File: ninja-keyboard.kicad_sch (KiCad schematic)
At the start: 143 parts, among them J1 USB_C_Receptacle_USB2.0_14P, J2 Conn_01x02, Q1 AO3401A, SW1 backquote, SW10 num9, SW11 num0, SW12 -, SW13 =, SW14 backsapce, SW15 tab, SW16 q, SW17 w, SW18 e, SW19 r, SW2 num1, SW20 t, SW21 y, SW22 u, SW23 i, SW24 o, SW25 p, SW26 [, SW27 ], SW28 \, SW29 cap, SW3 num2, SW30 a, SW31 s, SW32 d, SW33 f, SW34 h, SW35 g, SW36 j, SW37 k, SW38 l, SW39 semicolon, SW4 num3, SW40 apostrophe, SW41 enter, SW42 pgdown, SW43 lshift, SW44 z, SW45 x, SW46 c, SW47 v, SW48 b, SW49 n, SW5 num4, SW50 m, SW51 comma, SW52 period, SW53 /, SW54 rshift, SW55 up, SW56 end, SW57 lctrl, SW58 win, SW59 lalt, SW6 num5, SW60 lfn, SW61 space, SW62 macro, SW63 rfn, SW64 ralt, SW65 rctrl, SW66 left, SW67 down, SW68 right, SW69 pgup, SW7 num6, SW70 home, SW8 num7, SW9 num8, U1 ESP32-S3-WROOM-1, U2 AMS1117-3.3, U3 TP4056-42-ESOP8

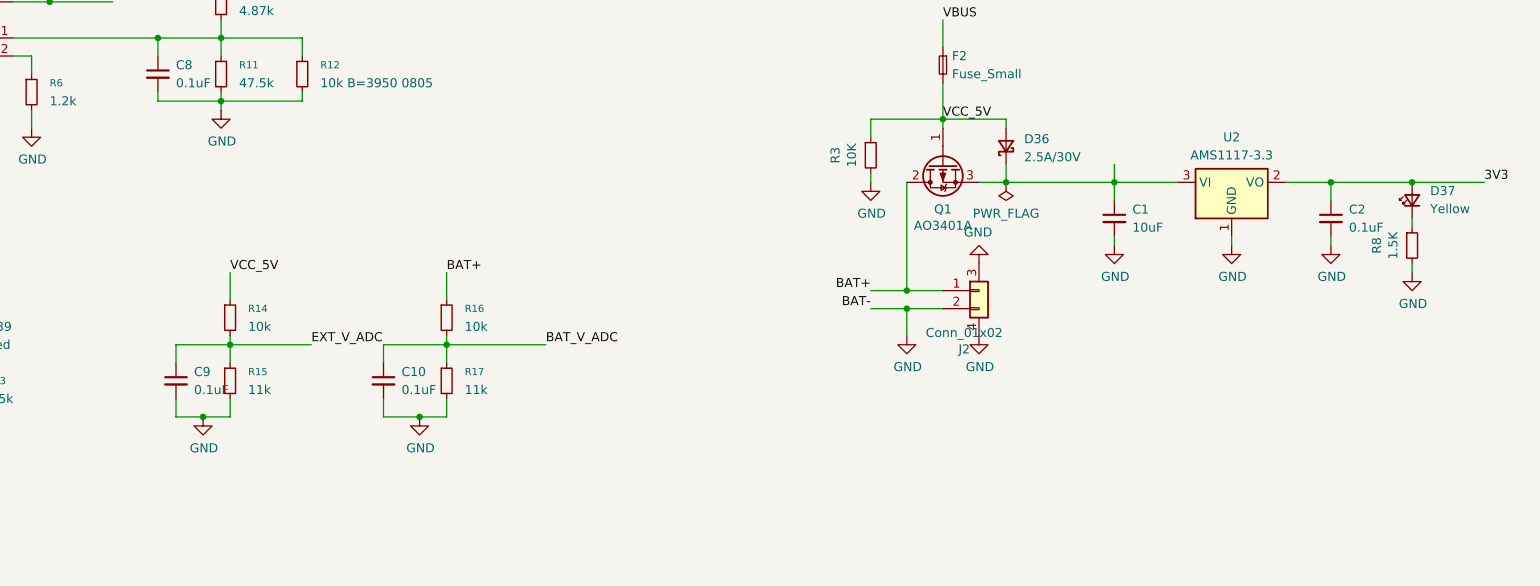
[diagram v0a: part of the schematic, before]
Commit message: Lay the components on the board, but haven't connect them with traces
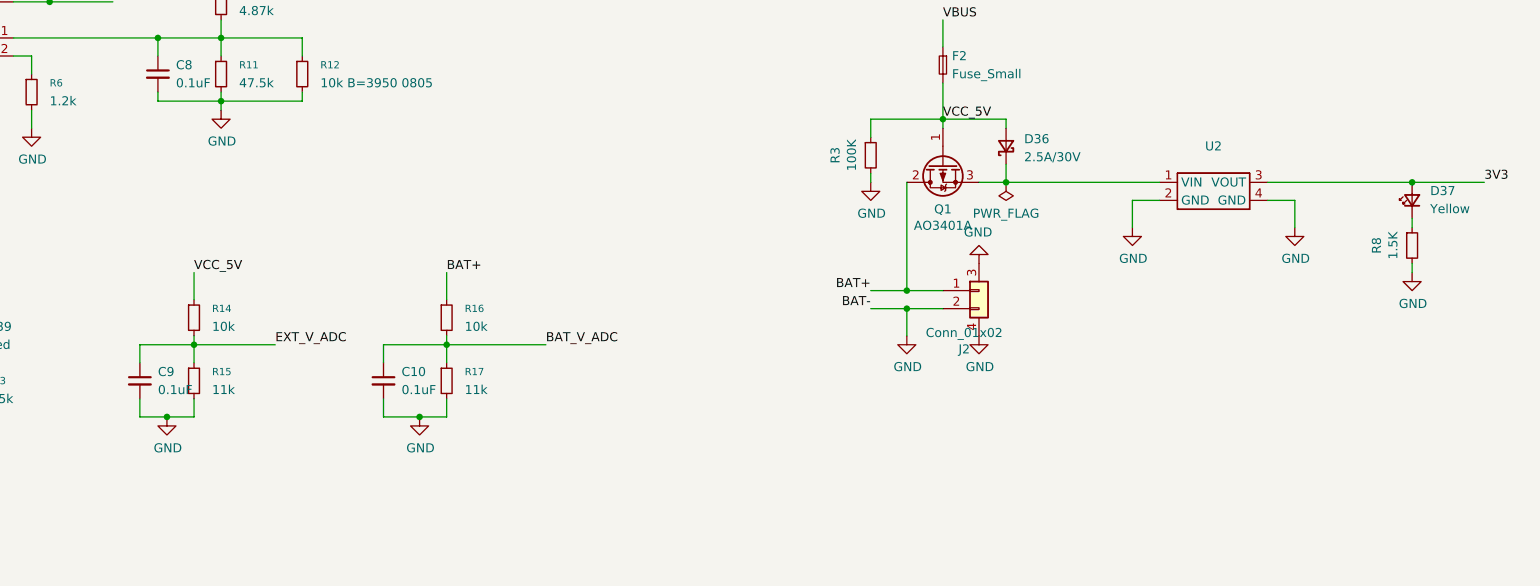
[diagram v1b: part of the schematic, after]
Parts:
- removed C1: 10uF, Capacitor_SMD:C_0603_1608Metric, symbol Device:C_Small
- removed C2: 0.1uF, Capacitor_SMD:C_0603_1608Metric, symbol Device:C_Small
- removed U2: AMS1117-3.3, Package_TO_SOT_SMD:SOT-223-3_TabPin2, symbol Regulator_Linear:AMS1117-3.3
- added U2: ~, user_added:XL63020-3.3, symbol user_created:XL63020-3.3
- R3: value 10K -> 100K
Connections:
- net 3V3: now also U2.3 (VOUT)
- net GND: now also U2.2 (GND), U2.4 (GND)
- net at D36.1 (K), Q1.3 (S): now also U2.1 (VIN)
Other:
- moved on the sheet: C9, R14, R15

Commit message: commit before trying to fix stuck kicad
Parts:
- SW1, SW10, SW11, SW12, SW13, SW16, SW17, SW18, SW19, SW2, SW20, SW21, SW22, SW23, SW24, SW25, SW26, SW27, SW3, SW30, SW31, SW32, SW33, SW34, SW35, SW36, SW37, SW38, SW39, SW4, SW40, SW42, SW44, SW45, SW46, SW47, SW48, SW49, SW5, SW50, SW51, SW52, SW53, SW55, SW56, SW6, SW60, SW63, SW66, SW67, SW68, SW69, SW7, SW70, SW8, SW9: symbol Switch:SW_Push -> user_created:SW_Push with Smart LED
- SW14, SW29: footprint PCM_Switch_Keyboard_Hotswap_Kailh:SW_Hotswap_Kailh_MX_1.75u -> user_added:SW_Hotswap_Kailh_MX_1.75u with led; symbol Switch:SW_Push -> user_created:SW_Push with Smart LED
- SW15, SW54: footprint PCM_Switch_Keyboard_Hotswap_Kailh:SW_Hotswap_Kailh_MX_1.50u -> user_added:SW_Hotswap_Kailh_MX_1.50u with led; symbol Switch:SW_Push -> user_created:SW_Push with Smart LED
- SW28, SW57, SW58, SW59, SW64, SW65: footprint PCM_Switch_Keyboard_Hotswap_Kailh:SW_Hotswap_Kailh_MX_1.25u -> user_added:SW_Hotswap_Kailh_MX_1.25u with led; symbol Switch:SW_Push -> user_created:SW_Push with Smart LED
- SW41: footprint PCM_Switch_Keyboard_Hotswap_Kailh:SW_Hotswap_Kailh_MX_2.00u -> user_added:SW_Hotswap_Kailh_MX_2.00u with led; symbol Switch:SW_Push -> user_created:SW_Push with Smart LED
- SW43, SW61, SW62: footprint PCM_Switch_Keyboard_Hotswap_Kailh:SW_Hotswap_Kailh_MX_2.25u -> user_added:SW_Hotswap_Kailh_MX_2.25u with led; symbol Switch:SW_Push -> user_created:SW_Push with Smart LED
- U1: footprint PCM_Espressif:ESP32-S3-WROOM-1U -> PCM_Espressif:ESP32-S3-WROOM-1
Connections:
- net GND: no longer J2.3, J2.4
- net at SW21.1, SW35.1, SW49.1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: now also SW21. (6), SW35. (6), SW49. (6), SW7. (6)
- net at SW20.2, SW34.2, SW48.2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: now also SW20. (6), SW34. (6), SW48. (6), SW6. (6)
- net at SW1.1, SW15.1, SW29.1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: now also SW1. (6), SW15. (6), SW29. (6), SW43. (6)
- net at SW13.1, SW27.1, SW41.1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: now also SW13. (6), SW27. (6), SW41. (6), SW55. (6)
- net at SW19.1, SW33.1, SW47.1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: now also SW19. (6), SW33. (6), SW47. (6), SW5. (6)
- net at SW23.1, SW37.1, SW51.1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: now also SW23. (6), SW37. (6), SW51. (6), SW9. (6)
- net at SW17.1, SW3.1, SW31.1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: now also SW17. (6), SW3. (6), SW31. (6), SW45. (6)
- net at SW14.2, SW28.2, SW42.2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: now also SW14. (6), SW28. (6), SW42. (6), SW56. (6)
- net at SW18.2, SW32.2, SW4.2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: now also SW18. (6), SW32. (6), SW4. (6), SW46. (6)
- net at SW22.2, SW36.2, SW50.2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: now also SW22. (6), SW36. (6), SW50. (6), SW8. (6)
- net at SW11.1, SW25.1, SW39.1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: now also SW11. (6), SW25. (6), SW39. (6), SW53. (6)
- net at SW12.2, SW26.2, SW40.2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: now also SW12. (6), SW26. (6), SW40. (6), SW54. (6)
- net at SW16.2, SW2.2, SW30.2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: now also SW16. (6), SW2. (6), SW30. (6), SW44. (6)
- net at SW10.2, SW24.2, SW38.2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: now also SW10. (6), SW24. (6), SW38. (6), SW52. (6)
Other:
- moved on the sheet: C10, C3, C4, C5, C6, C7, C8, C9, D1, D10, D11, D12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

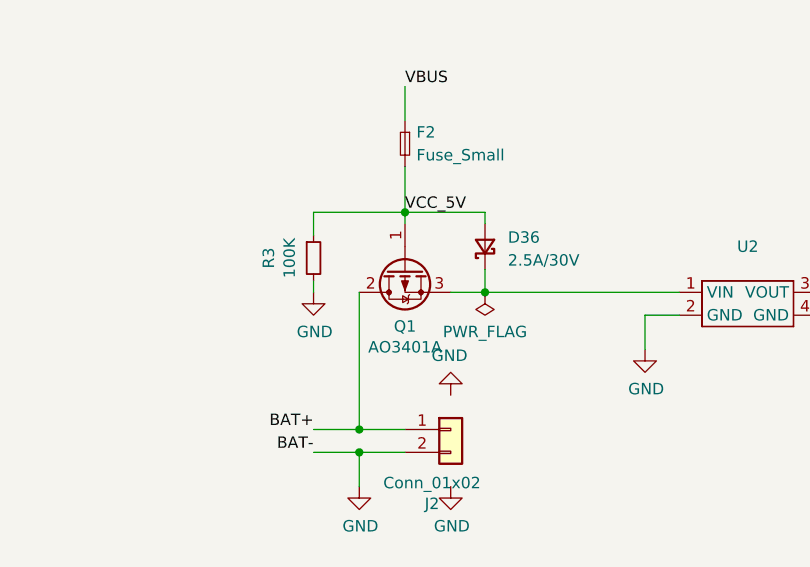
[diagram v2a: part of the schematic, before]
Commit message: use export netlist feature for now
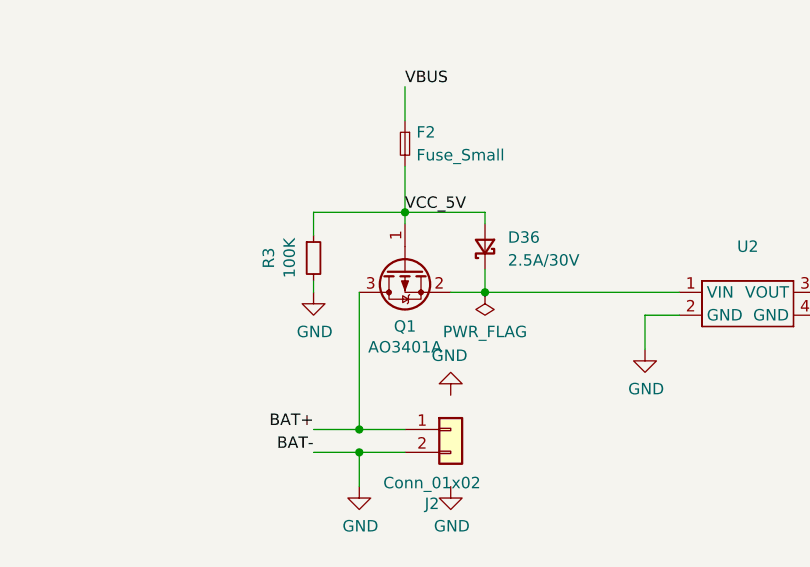
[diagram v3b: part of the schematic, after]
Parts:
- Q1: symbol Device:Q_PMOS_GDS -> Transistor_FET:AO3401A
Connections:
- net BAT+: now also Q1.3 (D); no longer Q1.2 (D)
- net at SW21.1, SW35.1, SW49.1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: now also SW21.3 (VDD), SW21.4 (DOUT), SW35.3 (VDD), SW35.4 (DOUT), SW49.3 (VDD), SW49.4 (DOUT), SW7.3 (VDD), SW7.4 (DOUT); no longer SW21. (6), SW35. (6), SW49. (6), SW7. (6)
- net at SW20.2, SW34.2, SW48.2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: now also SW20.5 (DIN), SW20.6 (GND), SW34.5 (DIN), SW34.6 (GND), SW48.5 (DIN), SW48.6 (GND), SW6.5 (DIN), SW6.6 (GND); no longer SW20. (6), SW34. (6), SW48. (6), SW6. (6)
- net at SW1.1, SW15.1, SW29.1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: now also SW1.3 (VDD), SW1.4 (DOUT), SW15.3 (VDD), SW15.4 (DOUT), SW29.3 (VDD), SW29.4 (DOUT), SW43.3 (VDD), SW43.4 (DOUT); no longer SW1. (6), SW15. (6), SW29. (6), SW43. (6)
- net at D36.1 (K), U2.1 (VIN): now also Q1.2 (S); no longer Q1.3 (S)
- net at SW13.1, SW27.1, SW41.1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: now also SW13.3 (VDD), SW13.4 (DOUT), SW27.3 (VDD), SW27.4 (DOUT), SW41.3 (VDD), SW41.4 (DOUT), SW55.3 (VDD), SW55.4 (DOUT); no longer SW13. (6), SW27. (6), SW41. (6), SW55. (6)
- net at SW19.1, SW33.1, SW47.1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: now also SW19.3 (VDD), SW19.4 (DOUT), SW33.3 (VDD), SW33.4 (DOUT), SW47.3 (VDD), SW47.4 (DOUT), SW5.3 (VDD), SW5.4 (DOUT); no longer SW19. (6), SW33. (6), SW47. (6), SW5. (6)
- net at SW23.1, SW37.1, SW51.1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: now also SW23.3 (VDD), SW23.4 (DOUT), SW37.3 (VDD), SW37.4 (DOUT), SW51.3 (VDD), SW51.4 (DOUT), SW9.3 (VDD), SW9.4 (DOUT); no longer SW23. (6), SW37. (6), SW51. (6), SW9. (6)
- net at SW17.1, SW3.1, SW31.1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: now also SW17.3 (VDD), SW17.4 (DOUT), SW3.3 (VDD), SW3.4 (DOUT), SW31.3 (VDD), SW31.4 (DOUT), SW45.3 (VDD), SW45.4 (DOUT); no longer SW17. (6), SW3. (6), SW31. (6), SW45. (6)
- net at SW14.2, SW28.2, SW42.2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: now also SW14.5 (DIN), SW14.6 (GND), SW28.5 (DIN), SW28.6 (GND), SW42.5 (DIN), SW42.6 (GND), SW56.5 (DIN), SW56.6 (GND); no longer SW14. (6), SW28. (6), SW42. (6), SW56. (6)
- net at SW18.2, SW32.2, SW4.2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: now also SW18.5 (DIN), SW18.6 (GND), SW32.5 (DIN), SW32.6 (GND), SW4.5 (DIN), SW4.6 (GND), SW46.5 (DIN), SW46.6 (GND); no longer SW18. (6), SW32. (6), SW4. (6), SW46. (6)
- net at SW22.2, SW36.2, SW50.2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: now also SW22.5 (DIN), SW22.6 (GND), SW36.5 (DIN), SW36.6 (GND), SW50.5 (DIN), SW50.6 (GND), SW8.5 (DIN), SW8.6 (GND); no longer SW22. (6), SW36. (6), SW50. (6), SW8. (6)
- net at SW11.1, SW25.1, SW39.1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: now also SW11.3 (VDD), SW11.4 (DOUT), SW25.3 (VDD), SW25.4 (DOUT), SW39.3 (VDD), SW39.4 (DOUT), SW53.3 (VDD), SW53.4 (DOUT); no longer SW11. (6), SW25. (6), SW39. (6), SW53. (6)
- net at SW12.2, SW26.2, SW40.2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: now also SW12.5 (DIN), SW12.6 (GND), SW26.5 (DIN), SW26.6 (GND), SW40.5 (DIN), SW40.6 (GND), SW54.5 (DIN), SW54.6 (GND); no longer SW12. (6), SW26. (6), SW40. (6), SW54. (6)
- net at SW16.2, SW2.2, SW30.2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: now also SW16.5 (DIN), SW16.6 (GND), SW2.5 (DIN), SW2.6 (GND), SW30.5 (DIN), SW30.6 (GND), SW44.5 (DIN), SW44.6 (GND); no longer SW16. (6), SW2. (6), SW30. (6), SW44. (6)
- net at SW10.2, SW24.2, SW38.2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: now also SW10.5 (DIN), SW10.6 (GND), SW24.5 (DIN), SW24.6 (GND), SW38.5 (DIN), SW38.6 (GND), SW52.5 (DIN), SW52.6 (GND); no longer SW10. (6), SW24. (6), SW38. (6), SW52. (6)

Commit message: Before add two inner layers and route with freeroute
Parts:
- added C11: 0.1uF, Capacitor_SMD:C_0603_1608Metric, symbol Device:C_Small
- added J3: Conn_01x05_Pin, Connector_PinHeader_2.54mm:PinHeader_1x05_P2.54mm_Vertical, symbol Connector:Conn_01x05_Pin
- added J4: ~, user_added:taobao 1x8 P0.5mm drawer bottom-side, symbol user_created:FPC_Connector_bottom_8_pin
- added Q2: SS8050, Package_TO_SOT_SMD:SOT-23, symbol Transistor_BJT:SS8050
- added R18: 47, Resistor_SMD:R_0603_1608Metric, symbol Device:R_Small
- added R19: 1K, Resistor_SMD:R_0603_1608Metric, symbol Device:R_Small
- added R20: 10K, Resistor_SMD:R_0603_1608Metric, symbol Device:R_Small
- added R21: 10R, Resistor_SMD:R_0603_1608Metric, symbol Device:R_Small
- R15: value 11k -> 13k
- U1: footprint PCM_Espressif:ESP32-S3-WROOM-1 -> PCM_Espressif:ESP32-S3-WROOM-1U
- U3: footprint Package_SO:SOIC-8-1EP_3.9x4.9mm_P1.27mm_EP2.41x3.3mm_ThermalVias -> Package_SO:SOIC-8-1EP_3.9x4.9mm_P1.27mm_EP2.41x3.3mm
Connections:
- net EXT_V_ADC is gone; now on net EXT_V_ON: C9.1, R14.2, R15.1
- net 3V3: now also SW1.3 (VDD), SW10.3 (VDD), SW11.3 (VDD), SW12.3 (VDD), SW13.3 (VDD), SW14.3 (VDD), SW15.3 (VDD), SW16.3 (VDD), SW17.3 (VDD), SW18.3 (VDD), SW19.3 (VDD), SW2.3 (VDD), SW20.3 (VDD), SW21.3 (VDD), SW22.3 (VDD), SW23.3 (VDD), SW24.3 (VDD), SW25.3 (VDD), SW26.3 (VDD), SW27.3 (VDD), SW28.3 (VDD), SW29.3 (VDD), SW3.3 (VDD), SW30.3 (VDD), SW31.3 (VDD), SW32.3 (VDD), SW33.3 (VDD), SW34.3 (VDD), SW35.3 (VDD), SW36.3 (VDD), SW37.3 (VDD), SW38.3 (VDD), SW39.3 (VDD), SW4.3 (VDD), SW40.3 (VDD), SW41.3 (VDD), SW42.3 (VDD), SW43.3 (VDD), SW44.3 (VDD), SW45.3 (VDD), SW46.3 (VDD), SW47.3 (VDD), SW48.3 (VDD), SW49.3 (VDD), SW5.3 (VDD), SW50.3 (VDD), SW51.3 (VDD), SW52.3 (VDD), SW53.3 (VDD), SW54.3 (VDD), SW55.3 (VDD), SW56.3 (VDD), SW57.3 (VDD), SW58.3 (VDD), SW59.3 (VDD), SW6.3 (VDD), SW60.3 (VDD), SW61.3 (VDD), SW62.3 (VDD), SW63.3 (VDD), SW64.3 (VDD), SW65.3 (VDD), SW66.3 (VDD), SW67.3 (VDD), SW68.3 (VDD), SW69.3 (VDD), SW7.3 (VDD), SW70.3 (VDD), SW8.3 (VDD), SW9.3 (VDD), C11.2, J4.2, R20.1
- net BAT_V_ADC: now also U1.5 (GPIO5/TOUCH5/ADC1_CH4)
- net CHARG_STATE: now also U1.7 (GPIO7/TOUCH7/ADC1_CH6)
- net GND: now also SW1.6 (GND), SW10.6 (GND), SW11.6 (GND), SW12.6 (GND), SW13.6 (GND), SW14.6 (GND), SW15.6 (GND), SW16.6 (GND), SW17.6 (GND), SW18.6 (GND), SW19.6 (GND), SW2.6 (GND), SW20.6 (GND), SW21.6 (GND), SW22.6 (GND), SW23.6 (GND), SW24.6 (GND), SW25.6 (GND), SW26.6 (GND), SW27.6 (GND), SW28.6 (GND), SW29.6 (GND), SW3.6 (GND), SW30.6 (GND), SW31.6 (GND), SW32.6 (GND), SW33.6 (GND), SW34.6 (GND), SW35.6 (GND), SW36.6 (GND), SW37.6 (GND), SW38.6 (GND), SW39.6 (GND), SW4.6 (GND), SW40.6 (GND), SW41.6 (GND), SW42.6 (GND), SW43.6 (GND), SW44.6 (GND), SW45.6 (GND), SW46.6 (GND), SW47.6 (GND), SW48.6 (GND), SW49.6 (GND), SW5.6 (GND), SW50.6 (GND), SW51.6 (GND), SW52.6 (GND), SW53.6 (GND), SW54.6 (GND), SW55.6 (GND), SW56.6 (GND), SW57.6 (GND), SW58.6 (GND), SW59.6 (GND), SW6.6 (GND), SW60.6 (GND), SW61.6 (GND), SW62.6 (GND), SW63.6 (GND), SW64.6 (GND), SW65.6 (GND), SW66.6 (GND), SW67.6 (GND), SW68.6 (GND), SW69.6 (GND), SW7.6 (GND), SW70.6 (GND), SW8.6 (GND), SW9.6 (GND), C11.1, J3.1 (Pin_1), J3.5 (Pin_5), J4.1, Q2.2 (E)
- net at SW21.5 (DIN): now also SW20.4 (DOUT)
- net GPIO37: now reaches D1.3 (K), D2.3 (K), D3.3 (K), D4.3 (K), D5.3 (K), D6.3 (K), D7.3 (K)
- net GPIO37: now also U1.30 (SPIDQS/GPIO37/FSPIQ/SUBSPIQ)
- net at SW1.5 (DIN): now also SW2.4 (DOUT)
- net at SW69.4 (DOUT): now also SW42.5 (DIN)
- net at SW69.5 (DIN): now also SW28.4 (DOUT)
- net at SW5.5 (DIN): now also SW6.4 (DOUT)
- net at SW48.4 (DOUT): now also SW49.5 (DIN)
- net GPIO48: now reaches D29.3 (K), D30.3 (K), D31.3 (K), D32.3 (K), D33.3 (K), D34.3 (K), D35.3 (K)
- net GPIO48: now also U1.25 (GPIO48/SPICLK_N/SUBSPICLK_N_DIFF)
- net at SW34.4 (DOUT): now also SW33.5 (DIN)
- net at SW37.5 (DIN): now also SW38.4 (DOUT)
- net GPIO35: now reaches D15.3 (K), D16.3 (K), D17.3 (K), D18.3 (K), D19.3 (K), D20.3 (K), D21.3 (K)
- net GPIO35: now also U1.28 (SPIIO6/GPIO35/FSPID/SUBSPID)
- net at SW31.5 (DIN): now also SW32.4 (DOUT)
- net at SW56.4 (DOUT): now also SW68.5 (DIN)
- net at SW70.4 (DOUT): now also SW14.5 (DIN)
- net at SW70.5 (DIN): now also R18.1
- net at SW22.4 (DOUT): now also SW23.5 (DIN)
- net at SW36.4 (DOUT): now also SW35.5 (DIN)
- net GPIO36: now reaches D10.3 (K), D11.3 (K), D12.3 (K), D13.3 (K), D14.3 (K), D8.3 (K), D9.3 (K)
- net GPIO36: now also U1.29 (SPIIO7/GPIO36/FSPICLK/SUBSPICLK)
- net at SW3.5 (DIN): now also SW4.4 (DOUT)
- net at SW39.5 (DIN): now also SW40.4 (DOUT)
- net at SW12.4 (DOUT): now also SW11.5 (DIN)
- net at SW41.5 (DIN): now also SW42.4 (DOUT)
- net at SW18.4 (DOUT): now also SW19.5 (DIN)
- net at SW59.4 (DOUT): now also SW58.5 (DIN)
- net at SW59.5 (DIN): now also SW60.4 (DOUT)
- net at SW58.4 (DOUT): now also SW57.5 (DIN)
- net at SW26.4 (DOUT): now also SW27.5 (DIN)
- net GPIO0: now reaches D22.3 (K), D23.3 (K), D24.3 (K), D25.3 (K), D26.3 (K), D27.3 (K), D28.3 (K)
- net GPIO0: now also U1.27 (GPIO0/BOOT), J3.2 (Pin_2)
- net at SW8.4 (DOUT): now also SW7.5 (DIN)
- net at SW68.4 (DOUT): now also SW67.5 (DIN)
- net at SW61.4 (DOUT): now also SW60.5 (DIN)
- net at SW61.5 (DIN): now also SW62.4 (DOUT)
- net at SW44.4 (DOUT): now also SW45.5 (DIN)
- net at SW66.4 (DOUT): now also SW65.5 (DIN)
- net at SW66.5 (DIN): now also SW67.4 (DOUT)
- net at SW63.4 (DOUT): now also SW62.5 (DIN)
- net at SW63.5 (DIN): now also SW64.4 (DOUT)
- net at SW65.4 (DOUT): now also SW64.5 (DIN)
- net at SW25.5 (DIN): now also SW24.4 (DOUT)
- net at SW46.4 (DOUT): now also SW47.5 (DIN)
- net at SW14.4 (DOUT): now also SW13.5 (DIN)
- net at SW55.5 (DIN): now also SW54.4 (DOUT)
- net at SW16.4 (DOUT): now also SW17.5 (DIN)
- net at SW51.5 (DIN): now also SW50.4 (DOUT)
- net GPIO17: now reaches U1.10 (GPIO17/U1TXD/ADC2_CH6)
- net GPIO17: now also SW12.2, SW26.2, SW40.2, SW54.2, SW68.2
- net GPIO18: now reaches U1.11 (GPIO18/U1RXD/ADC2_CH7/CLK_OUT3)
- net GPIO18: now also SW11.1, SW25.1, SW39.1, SW53.1, SW67.1
- net GPIO8: now reaches U1.12 (GPIO8/TOUCH8/ADC1_CH7/SUBSPICS1)
- net GPIO8: now also SW10.2, SW24.2, SW38.2, SW52.2, SW66.2
- net LCD_RST: now reaches U1.17 (GPIO9/TOUCH9/ADC1_CH8/FSPIHD/SUBSPIHD)
- net LCD_RST: now also J4.5
- net LCD_CS: now reaches U1.18 (GPIO10/TOUCH10/ADC1_CH9/FSPICS0/FSPIIO4/SUBSPICS0)
- net LCD_CS: now also J4.7
- net LCD_SDA: now reaches U1.19 (GPIO11/TOUCH11/ADC2_CH0/FSPID/FSPIIO5/SUBSPID)
- net LCD_SDA: now also J4.4
- net LCD_SCL: now reaches U1.20 (GPIO12/TOUCH12/ADC2_CH1/FSPICLK/FSPIIO6/SUBSPICLK)
- net LCD_SCL: now also J4.3
- net LCD_DC: now reaches U1.21 (GPIO13/TOUCH13/ADC2_CH2/FSPIQ/FSPIIO7/SUBSPIQ)
- net LCD_DC: now also J4.6
- net LCD_BLK: now reaches U1.22 (GPIO14/TOUCH14/ADC2_CH3/FSPIWP/FSPIDQS/SUBSPIWP)
- net LCD_BLK: now also R19.1
- net GPIO21: now reaches U1.23 (GPIO21)
- net GPIO21: now also SW23.1, SW37.1, SW51.1, SW65.1, SW9.1
- net GPIO47: now reaches U1.24 (GPIO47/SPICLK_P/SUBSPICLK_P_DIFF)
- net GPIO47: now also SW22.2, SW36.2, SW50.2, SW64.2, SW8.2
- net GPIO38: now reaches U1.31 (GPIO38/FSPIWP/SUBSPIWP)
- net GPIO38: now also SW21.1, SW35.1, SW49.1, SW63.1, SW7.1
- net GPIO39: now reaches U1.32 (MTCK/GPIO39/CLK_OUT3/SUBSPICS1)
- net GPIO39: now also SW20.2, SW34.2, SW48.2, SW6.2, SW62.2
- net GPIO40: now reaches U1.33 (MTDO/GPIO40/CLK_OUT2)
- net GPIO40: now also SW19.1, SW33.1, SW47.1, SW5.1, SW61.1
- net GPIO41: now reaches U1.34 (MTDI/GPIO41/CLK_OUT1)
- net GPIO41: now also SW18.2, SW32.2, SW4.2, SW46.2, SW60.2
- net GPIO42: now reaches U1.35 (MTMS/GPIO42)
- net GPIO42: now also SW17.1, SW3.1, SW31.1, SW45.1, SW59.1
- net RXD0: now reaches U1.36 (U0RXD/GPIO44/CLK_OUT2)
- net RXD0: now also J3.4 (Pin_4)
- net TXD0: now reaches U1.37 (U0TXD/GPIO43/CLK_OUT1)
- net TXD0: now also J3.3 (Pin_3)
- net GPIO2: now reaches U1.38 (GPIO2/TOUCH2/ADC1_CH1)
- net GPIO2: now also SW16.2, SW2.2, SW30.2, SW44.2, SW58.2
- net GPIO1: now reaches U1.39 (GPIO1/TOUCH1/ADC1_CH0)
- net GPIO1: now also SW1.1, SW15.1, SW29.1, SW43.1, SW57.1
- net LED_DRV: now reaches U1.4 (GPIO4/TOUCH4/ADC1_CH3)
- net LED_DRV: now also R18.2
- net EXT_V_ON: now reaches U1.6 (GPIO6/TOUCH6/ADC1_CH5)
- net GPIO15: now reaches U1.8 (GPIO15/U0RTS/ADC2_CH4/XTAL_32K_P)
- net GPIO15: now also SW14.2, SW28.2, SW42.2, SW56.2, SW70.2
- net GPIO16: now reaches U1.9 (GPIO16/U0CTS/ADC2_CH5/XTAL_32K_N)
- net GPIO16: now also SW13.1, SW27.1, SW41.1, SW55.1, SW69.1
- net at SW15.5 (DIN): now also SW1.4 (DOUT)
- net at SW9.5 (DIN): now also SW10.4 (DOUT)
- net at SW52.4 (DOUT): now also SW53.5 (DIN)
- net at SW29.5 (DIN): now also SW30.4 (DOUT)
- net at SW43.5 (DIN): now also SW29.4 (DOUT)
- new net: SW21.4 (DOUT), SW22.5 (DIN)
- new net: SW19.4 (DOUT), SW20.5 (DIN)
- new net: Q2.1 (B), R19.2, R20.2
- new net: SW4.5 (DIN), SW5.4 (DOUT)
- new net: SW47.4 (DOUT), SW48.5 (DIN)
- new net: SW34.5 (DIN), SW35.4 (DOUT)
- new net: SW36.5 (DIN), SW37.4 (DOUT)
- new net: SW30.5 (DIN), SW31.4 (DOUT)
- new net: SW55.4 (DOUT), SW56.5 (DIN)
- new net: SW32.5 (DIN), SW33.4 (DOUT)
- new net: SW27.4 (DOUT), SW28.5 (DIN)
- new net: SW2.5 (DIN), SW3.4 (DOUT)
- new net: SW38.5 (DIN), SW39.4 (DOUT)
- new net: SW12.5 (DIN), SW13.4 (DOUT)
- new net: SW40.5 (DIN), SW41.4 (DOUT)
- new net: SW17.4 (DOUT), SW18.5 (DIN)
- new net: SW25.4 (DOUT), SW26.5 (DIN)
- new net: SW8.5 (DIN), SW9.4 (DOUT)
- new net: SW43.4 (DOUT), SW44.5 (DIN)
- new net: SW49.4 (DOUT), SW50.5 (DIN)
- new net: SW45.4 (DOUT), SW46.5 (DIN)
- new net: SW23.4 (DOUT), SW24.5 (DIN)
- new net: SW15.4 (DOUT), SW16.5 (DIN)
- new net: SW51.4 (DOUT), SW52.5 (DIN)
- new net: SW53.4 (DOUT), SW54.5 (DIN)
- new net: SW10.5 (DIN), SW11.4 (DOUT)
- new net: Q2.3 (C), R21.1
- new net: SW6.5 (DIN), SW7.4 (DOUT)
- new net LCD_LEDK: J4.8, R21.2
- no-connect marks 0 -> 4
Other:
- note added: "Peripherals"

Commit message: Add a rotatory encoder and a switch for battery
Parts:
- added C1, C2: 0.1uF, Capacitor_SMD:C_0603_1608Metric, symbol Device:C_Small
- added R22, R23: 13K, Resistor_SMD:R_0603_1608Metric, symbol Device:R_Small
- added SW71: RotaryEncoder, Rotary_Encoder:RotaryEncoder_Alps_EC12E_Vertical_H20mm, symbol Device:RotaryEncoder
- added SW72: SW_SPDT, Button_Switch_SMD:SW_SPDT_CK_JS102011SAQN, symbol Switch:SW_SPDT
- R10: value 4.87k -> 4.87K
- R11: value 47.5k -> 47.5K
- R13: value 1.5k -> 1.5K
- R14, R16: value 10k -> 10K
- R15: value 13k -> 13K
- R17: value 11k -> 11K
- R6: value 1.2k -> 1.2K
- R9: value 3k -> 3K
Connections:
- net 3V3: now also R22.1, R23.1
- net BAT+: now also SW72.3 (C); no longer J2.1 (Pin_1)
- net GND: now also C1.2, C2.2, SW71.C
- net GPIO21: now also C1.1, R22.2, SW71.A; no longer SW23.1, SW37.1, SW51.1, SW65.1, SW9.1
- net GPIO47: now also C2.1, R23.2, SW71.B; no longer SW22.2, SW36.2, SW50.2, SW64.2, SW8.2
- net GPIO3: now reaches U1.15 (GPIO3/TOUCH3/ADC1_CH2)
- net GPIO3: now also SW23.1, SW37.1, SW51.1, SW65.1, SW9.1
- net GPIO46: now reaches U1.16 (GPIO46)
- net GPIO46: now also SW22.2, SW36.2, SW50.2, SW64.2, SW8.2
- new net: J2.1 (Pin_1), SW72.2 (B)
- no-connect marks 4 -> 3
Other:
- moved on the sheet: J2

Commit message: Remove fuse
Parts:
- removed F2: Fuse_Small, Fuse:Fuse_0805_2012Metric, symbol Device:Fuse_Small
- C1, C10, C2, C8, C9: LCSC Part # (none) -> C14663
- C6, C7: LCSC Part # (none) -> C19702
- D1, D10, D11, D12, D13, D14, D15, D16, D17, D18, D19, D2, D20, D21, D22, D23, D24, D25, D26, D27, D28, D29, D3, D30, D31, D32, D33, D34, D35, D4, D5, D6, D7, D8, D9: value ~ -> DAV70; LCSC Part # (none) -> C68978
- D37: LCSC Part # C2286 -> C2296
- D38: LCSC Part # (none) -> C2297
- D39: LCSC Part # (none) -> C2286
- R1, R2: LCSC Part # (none) -> C23345
- R10: LCSC Part # (none) -> C23045
- R11: LCSC Part # (none) -> C23061
- R12: LCSC Part # (none) -> C95968
- R13: LCSC Part # (none) -> C22843
- R14, R16: LCSC Part # (none) -> C25804
- R15, R22, R23: LCSC Part # (none) -> C22797
- R17: LCSC Part # (none) -> C25950
- R18: LCSC Part # (none) -> C23182
- R19: LCSC Part # (none) -> C21190
- R21: LCSC Part # (none) -> C22859
- R3: LCSC Part # C25804 -> C25803
- R6: LCSC Part # (none) -> C22765
- R8: LCSC Part # C25804 -> C22843
- R9: LCSC Part # (none) -> C4211
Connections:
- net VCC_5V is gone; now on net VBUS: C6.1, D36.2 (A), D38.2 (A), Q1.1 (G), R10.1, R14.1, R3.1, U3.4 (V_{CC}), U3.8 (CE)
